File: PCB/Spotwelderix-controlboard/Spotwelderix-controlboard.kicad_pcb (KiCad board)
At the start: 2 copper layers, 60.4 x 70 mm, 45 parts, among them J1 LEDs, J2 ChargerPower, J3 ExtPwr_FAn, J4 Testpin, P1 Display, P2 CONN_01X08, Q1 AO3400A, Q2 AO3400A, Q3 AO3400A, U1 NodeMCU32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

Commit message: v4
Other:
- board text added: "FtSwt-ExtPwr"
- board text removed: "ExtPwr-FtSwt"

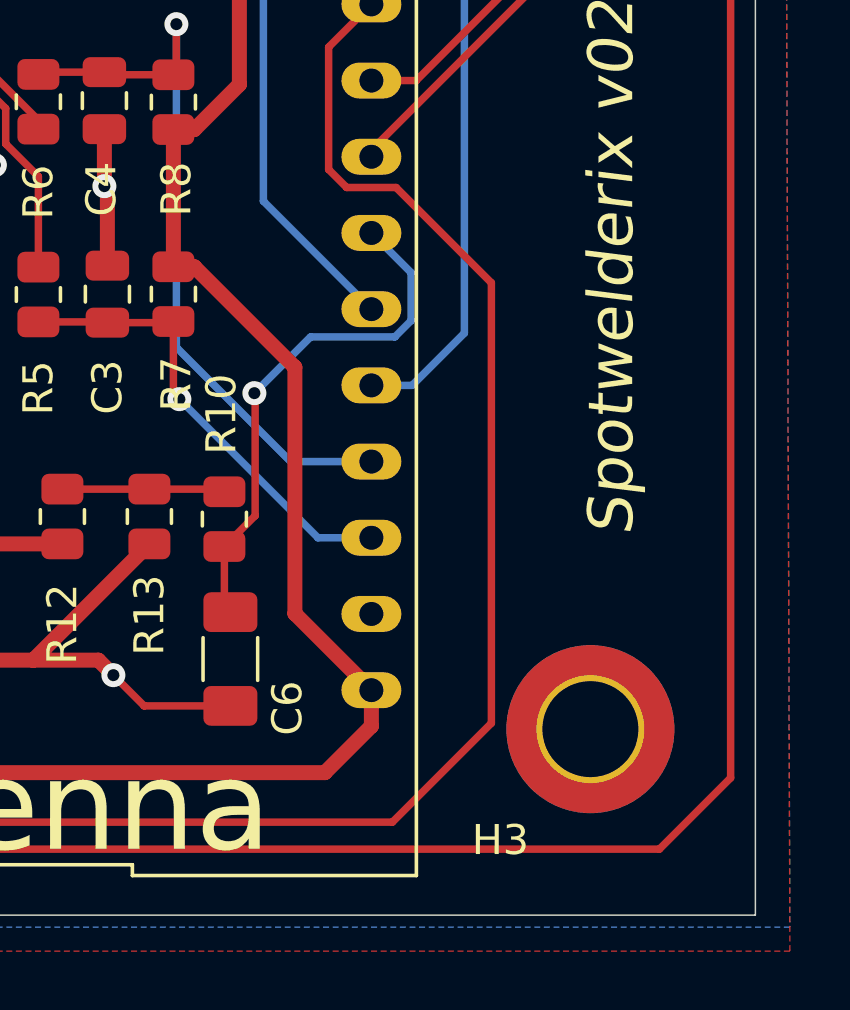
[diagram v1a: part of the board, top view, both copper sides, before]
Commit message: v3 commissioning
v3 has updated measurment devices to allow measurment of 1kA and voltages down to 0.3V accurately. Measeure the short!
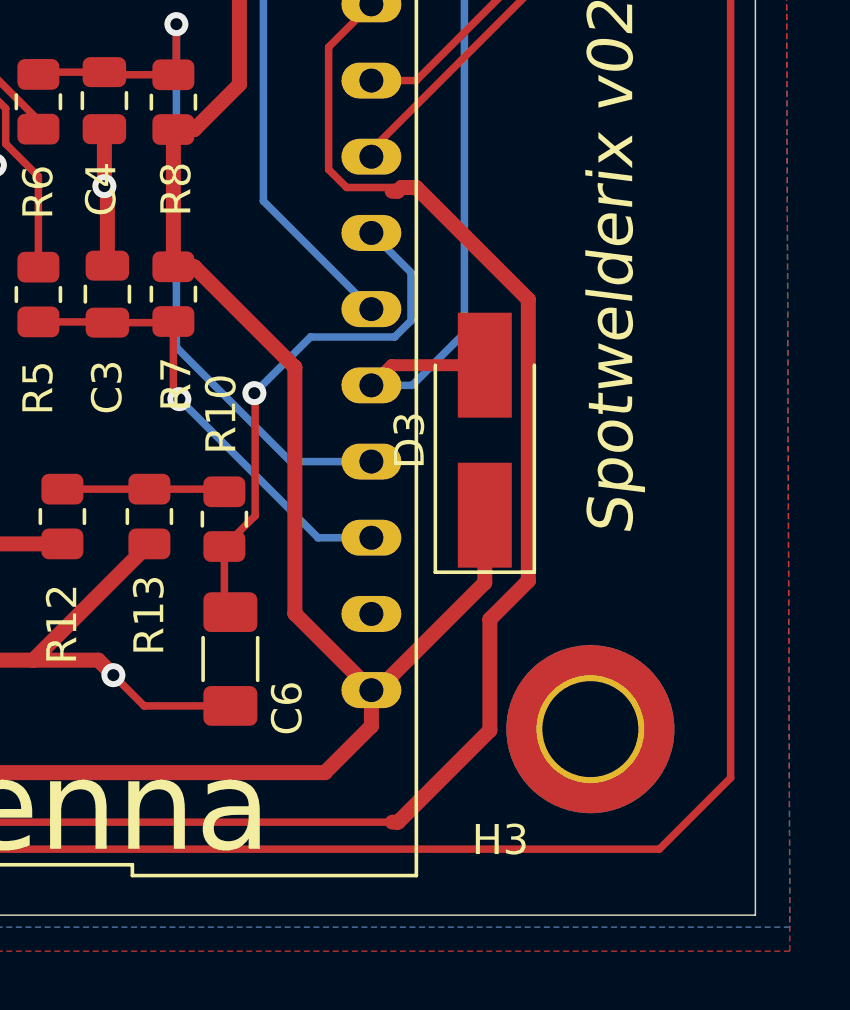
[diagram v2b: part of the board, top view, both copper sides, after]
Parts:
- added D3: D_Schottky, Diode_SMD:D_SMA_Handsoldering, F.Cu at (76.6, 74.2)
- R17: value 100 -> 10k
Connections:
- net Vbat_ADC renamed Probe_diff
- J4 pad 4: +3V3 -> +5V
- P2 pad 6: +3V3 -> +5V
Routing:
- net +3V3: track 173.3 -> 180.8 mm
- net Probe_diff: track 46.5 -> 50.6 mm
- net BUZZ: track 67.6 -> 69.3 mm
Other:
- net class Default: trace_width 0.25 -> 0.4
